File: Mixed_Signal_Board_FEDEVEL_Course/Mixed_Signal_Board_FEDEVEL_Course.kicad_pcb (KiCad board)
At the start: 4 copper layers, 116 parts, among them J200 USB_C_Receptacle_USB2.0_16P, J201 Conn_02x03_Counter_Clockwise, J300 031-5640-1010, J400 031-5640-1010, SW1 SW_Push, U1 REF3033AIDBZT, U100 HT7533-1, U101 TLV62569DBVR, U102 MCP6001T-E/OT, U200 STM32F103C8T6, U201 USBLC6-2SC6, U300 ADC141S626CIMM_NOPB, U301 MCP6001T-E/OT, U302 MCP6001T-E/OT, U400 DAC7563SDGSR, U401 MCP6001T-E/OT, Y200 X322516MLB4SI

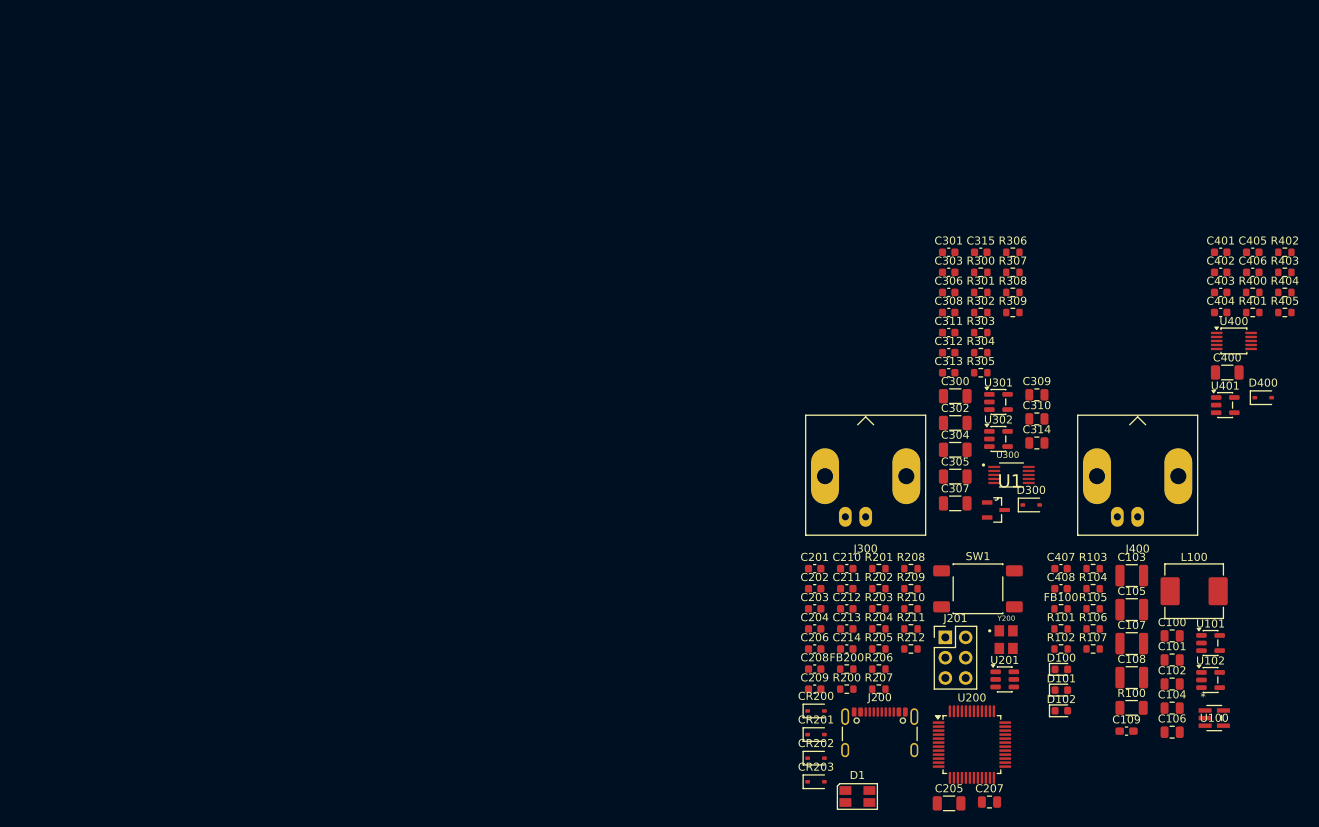
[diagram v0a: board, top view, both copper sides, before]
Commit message: Add the placement of the MCU sheet
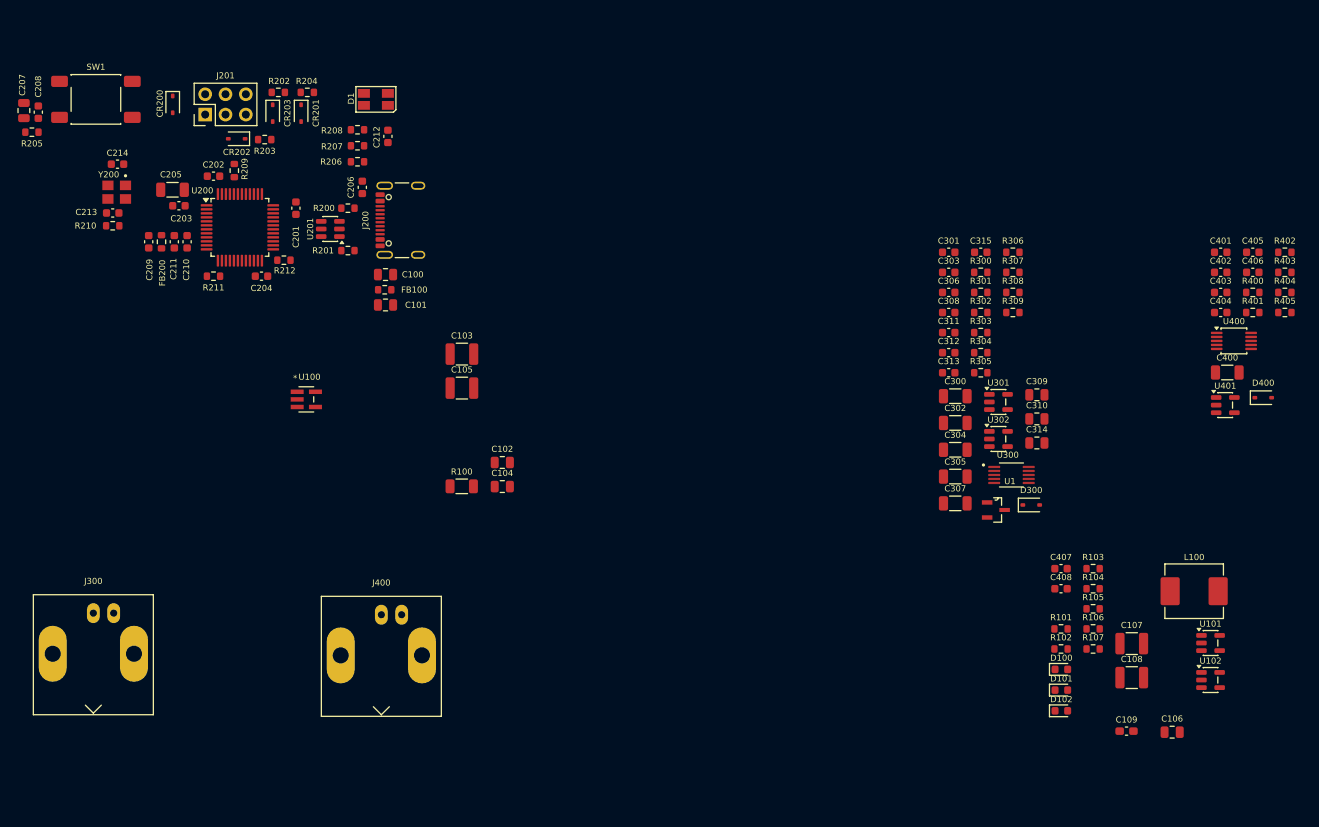
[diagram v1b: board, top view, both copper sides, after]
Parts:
- moved C207 148.5 mm to (34.6, 45.8), turned to 90 degrees
- moved SW1 126.1 mm to (43.6, 44.4)
- moved Y200 124.5 mm to (46.2, 56.0), turned to -90 degrees
- moved R205 124.0 mm to (35.6, 48.5), turned to 180 degrees
- moved C205 123.7 mm to (53.2, 55.7), turned to 180 degrees
- moved U100 120.3 mm to (69.9, 81.9)
- moved C208 119.4 mm to (36.4, 46.0), turned to -90 degrees
- moved J201 113.3 mm to (57.3, 46.3), turned to 90 degrees
- moved U200 112.0 mm to (61.6, 60.4)
- moved R210 110.7 mm to (45.7, 60.2)
- moved CR200 110.5 mm to (53.2, 45.0), turned to -90 degrees
- moved C214 109.5 mm to (46.3, 52.5)
- moved C100 108.2 mm to (79.8, 66.3), turned to 180 degrees
- moved C101 107.9 mm to (79.8, 70.1)
- moved CR203 107.7 mm to (65.7, 46.1), turned to -90 degrees
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
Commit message: Complete the placement of the board
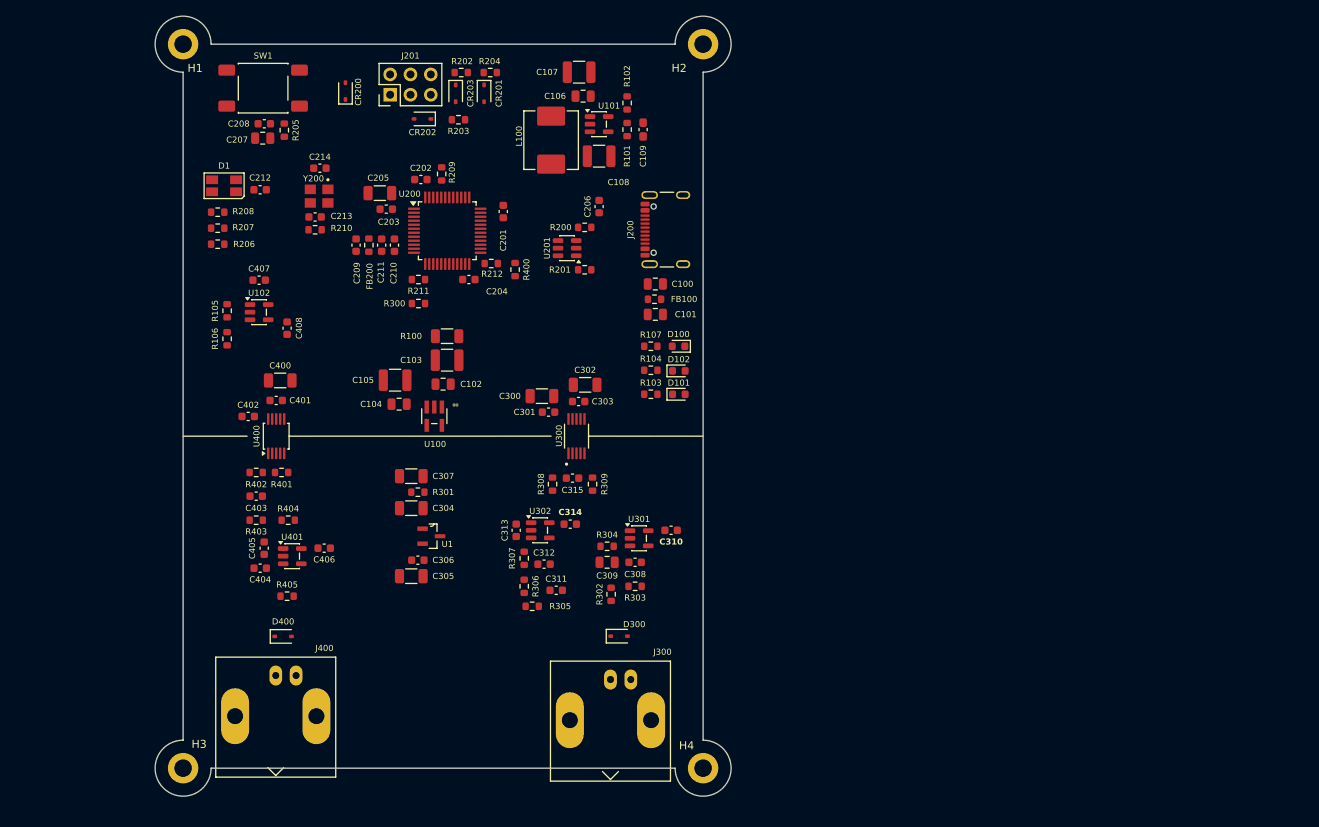
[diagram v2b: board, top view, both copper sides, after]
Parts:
- added H1: MountingHole_Pad, MountingHole:MountingHole_2.2mm_M2_DIN965_Pad, F.Cu at (54.5, 37.5)
- added H2: MountingHole_Pad, MountingHole:MountingHole_2.2mm_M2_DIN965_Pad, F.Cu at (119.5, 37.5)
- added H3: MountingHole_Pad, MountingHole:MountingHole_2.2mm_M2_DIN965_Pad, F.Cu at (54.5, 128.0)
- added H4: MountingHole_Pad, MountingHole:MountingHole_2.2mm_M2_DIN965_Pad, F.Cu at (119.5, 128.0)
- C310, C314: footprint Capacitor_SMD:C_0805_2012Metric -> Capacitor_SMD:C_0603_1608Metric
- moved R403 132.3 mm to (63.6, 97.0), turned to 180 degrees
- moved R402 131.5 mm to (63.6, 91.0)
- moved R405 129.7 mm to (67.5, 106.5)
- moved C405 129.0 mm to (64.6, 100.5), turned to -90 degrees
- moved R404 127.8 mm to (67.6, 97.0)
- moved U102 127.5 mm to (64.0, 71.0)
- moved D400 126.1 mm to (67.0, 111.5)
- moved C404 124.2 mm to (64.1, 103.0), turned to 180 degrees
- moved C403 123.2 mm to (63.6, 94.0), turned to 180 degrees
- moved R401 123.0 mm to (66.8, 91.0)
- moved C402 122.9 mm to (62.6, 84.0)
- moved C406 121.1 mm to (72.1, 100.5), turned to 180 degrees
- moved U400 120.3 mm to (66.1, 86.5), turned to 90 degrees
- moved C401 119.5 mm to (66.1, 82.0)
- moved C400 118.4 mm to (66.6, 79.5)
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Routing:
- added copper zone on In1.Cu, net GND
- added copper zone on In2.Cu, net GND
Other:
- board outline added: 72 x 97.5 mm

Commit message: Finalizing the layout of the board
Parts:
- moved C307 13.3 mm to (85.5, 104.5), turned to 0 degrees
- moved C305 12.2 mm to (85.5, 92.0), turned to 180 degrees
- moved R301 9.09 mm to (84.7, 102.5), turned to 0 degrees
- moved C306 8.00 mm to (84.7, 94.0), turned to 180 degrees
- moved R404 5.97 mm to (62.8, 100.5), turned to 90 degrees
- moved C304 5.65 mm to (85.5, 100.5), turned to 0 degrees
- moved C206 4.10 mm to (102.4, 57.8)
- moved C400 3.21 mm to (63.4, 79.5), turned to 180 degrees
- moved U1 3.15 mm to (83.0, 97.0), turned to 180 degrees
- moved D101 3.06 mm to (116.5, 78.2), turned to 180 degrees
- moved R103 3.06 mm to (113.0, 78.2)
- moved D102 2.84 mm to (116.5, 81.2), turned to 180 degrees
- moved R104 2.84 mm to (113.0, 81.1)
- moved CR200 2.11 mm to (74.8, 45.5), turned to -90 degrees
- moved C401 1.87 mm to (64.3, 81.8), turned to 180 degrees
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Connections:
- U200 pad 20: /DAC_NCLR -> /DAC_NLDAC
- U200 pad 21: /DAC_NLDAC -> /DAC_NCLR
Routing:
- net +3.3V: track 0.00 -> 192.8 mm, vias 0 -> 13
- net GND: track 0.00 -> 161.4 mm, vias 0 -> 171
- net +3.3VA: track 0.00 -> 153.7 mm, vias 0 -> 4
- net V_BUS: track 0.00 -> 107.9 mm, vias 0 -> 4
- net V_BUS_Filtered: track 0.00 -> 83.4 mm, vias 0 -> 2
- net VCOM: track 0.00 -> 77.0 mm, vias 0 -> 3
- net /Mixed_Signal_Board_MCU/NRST: track 0.00 -> 58.1 mm
- net /SPI_CS: track 0.00 -> 42.7 mm, vias 0 -> 2
- net /Mixed_Signal_Board_DAC/DAC_SCLK: track 0.00 -> 39.7 mm, vias 0 -> 2
- net /SPI2_NSS: track 0.00 -> 37.1 mm, vias 0 -> 2
- net /SPI2_MOSI: track 0.00 -> 36.5 mm
- net /Mixed_Signal_Board_MCU/TIM4_CH1: track 0.00 -> 34.7 mm, vias 0 -> 2
- net /DAC_NLDAC: track 0.00 -> 33.6 mm
- net Net-(U300-SCLK): track 0.00 -> 33.1 mm, vias 0 -> 2
- net /DAC_NCLR: track 0.00 -> 32.9 mm
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- added copper zone on B.Cu, net +3.3V
- added copper zone on F.Cu, net +3.3V
- added copper zone on F.Cu, net +3.3VA
- added copper zone on F.Cu, net GND
- added copper zone on F.Cu, net Net-(U100-VIN)
- added copper zone on F.Cu, net V_BUS_Filtered
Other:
- board size 72 x 97.5 mm -> 72.1 x 99 mm
- board text added: "ADC circuit"
- board text added: "Active LPF"
- board text added: "Analoge signal Input"
- board text added: "Analoge signal output"
- board text added: "Buck Converter"
- board text added: "DAC circuit"
- board text added: "Debugger"
- board text added: "PWR LEDS"
- board text added: "RGB LED"
- board text added: "Reset"
- board text added: "USB-C Interface"
- board text added: "Voltage Referance"
